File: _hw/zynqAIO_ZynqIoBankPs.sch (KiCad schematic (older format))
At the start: 70 parts, among them J201 Conn_01x03_Male, J202 Conn_01x03_Male, U201 xc7z010clg400, U202 DSC1121

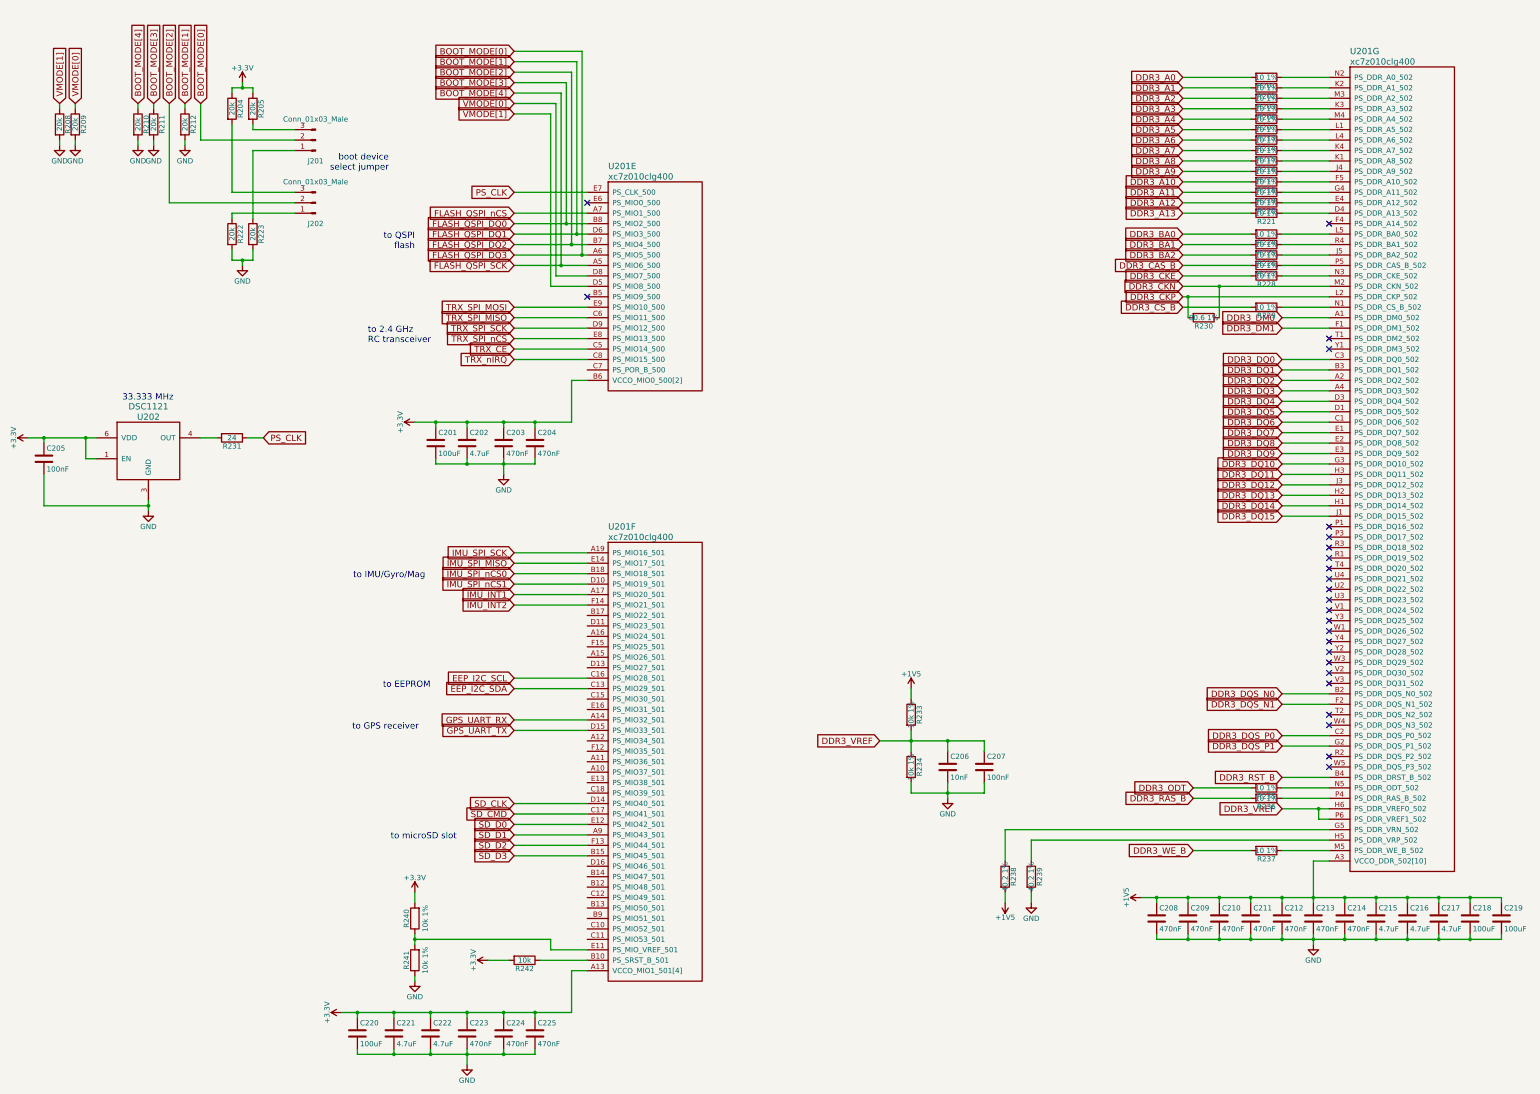
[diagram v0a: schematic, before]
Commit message: Removed Zybo board part. Not needed and complicates project setup.
Configured DDR3 to 16-bit width (using only 1 of the 2 DDR3 chips on Zybo but aligned more to zynqFC configuration).

Disabled Ethernet/USB. Not part of zynqFC.

Enabled SPI0 peripheral for IMU, I²C1 peripheral for EEPROM and UART0 peripheral for GPS.
However, all three interfaces cannot be used on Zybo and will not be used in SW.

Updated HW pinning to current Zynq PS bank planning.
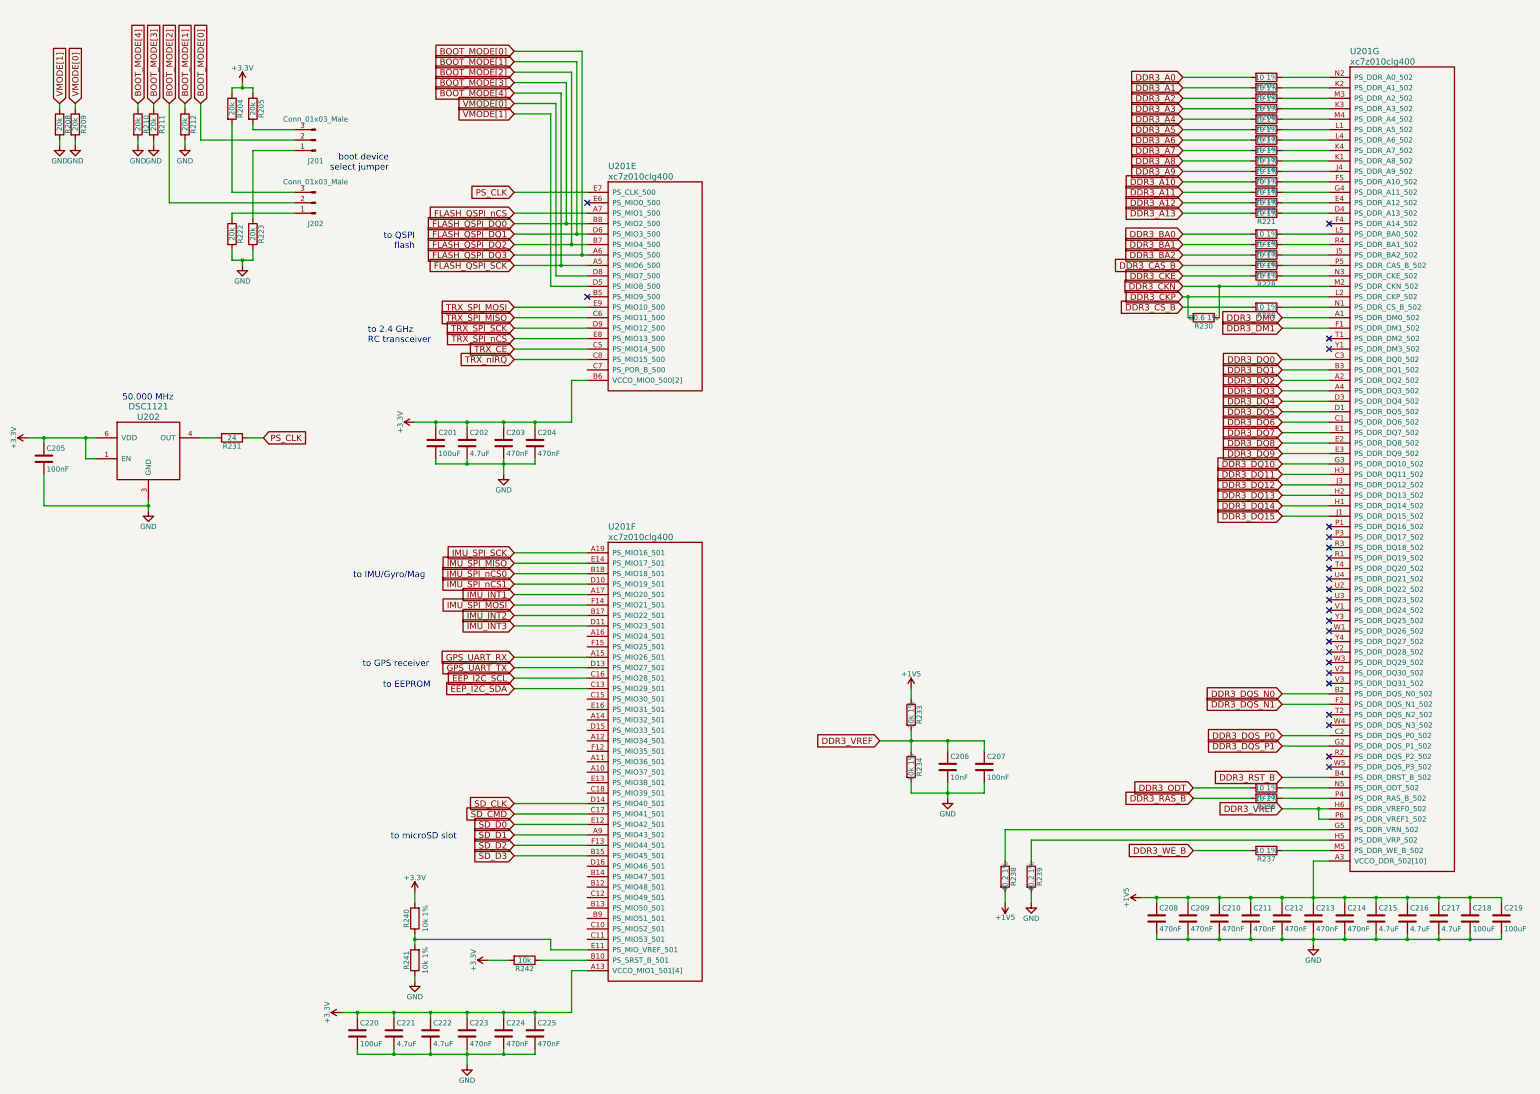
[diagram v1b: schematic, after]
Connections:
- net GPS_UART_RX: now also U201.A15 (PS_MIO26_501); no longer U201.A14 (PS_MIO32_501)
- net GPS_UART_TX: now also U201.D13 (PS_MIO27_501); no longer U201.D15 (PS_MIO33_501)
- net IMU_INT2: now also U201.B17 (PS_MIO22_501); no longer U201.F14 (PS_MIO21_501)
- net IMU_INT3: now reaches U201.D11 (PS_MIO23_501)
- new net IMU_SPI_MOSI: U201.F14 (PS_MIO21_501)
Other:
- note added: "50.000 MHz"
- note removed: "33.333 MHz"
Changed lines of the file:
@@
 Text GLabel 5450 6300 0    60   Input ~ 0
 IMU_INT1
-Text GLabel 5450 6400 0    60   Input ~ 0
+Text GLabel 5450 6500 0    60   Input ~ 0
 IMU_INT2
 Text GLabel 12800 4050 0    60   Input ~ 0
@@
 	4700 5000 4700 5050
 Wire Wire Line
-	4700 5050 5650 5050
+	4700 5050 5000 5050
 Wire Wire Line
 	5650 5050 5650 5000
 Wire Wire Line
-	5350 5000 5350 5150
+	5350 5000 5350 5050
 Connection ~ 5350 5050
 Wire Wire Line
@@
 Connection ~ 5000 5050
 Wire Wire Line
-	4500 4650 6000 4650
+	4500 4650 4700 4650
 Wire Wire Line
 	6000 4650 6000 4250
@@
 Connection ~ 4700 4650
 Wire Wire Line
-	3950 10700 5650 10700
+	3950 10700 4300 10700
 Wire Wire Line
 	5650 10700 5650 10650
@@
 Connection ~ 5350 10700
 Wire Wire Line
-	5000 10650 5000 10800
+	5000 10650 5000 10700
 Connection ~ 5000 10700
 Wire Wire Line
-	3800 10300 6000 10300
+	3800 10300 3950 10300
 Wire Wire Line
 	6000 10300 6000 9900
@@
 	5800 9600 4500 9600
 Wire Wire Line
-	4500 9550 4500 9650
+	4500 9550 4500 9600
 Connection ~ 4500 9600
 Wire Wire Line
@@
 	6150 4050 5450 4050
 Wire Wire Line
-	5450 3150 6150 3150
+	5450 3150 5900 3150
 Wire Wire Line
 	5450 2650 6150 2650
 Wire Wire Line
-	5450 2750 6150 2750
-Wire Wire Line
-	5450 2850 6150 2850
-Wire Wire Line
-	5450 2950 6150 2950
-Wire Wire Line
-	5450 3050 6150 3050
+	5450 2750 5950 2750
+Wire Wire Line
+	5450 2850 6050 2850
+Wire Wire Line
+	5450 2950 6000 2950
+Wire Wire Line
+	5450 3050 6100 3050
 Wire Wire Line
 	6100 1100 6100 3050
@@
 	2750 3000 2750 3100
 Wire Wire Line
-	2750 3100 2950 3100
+	2750 3100 2850 3100
 Wire Wire Line
 	2950 3100 2950 3000
@@
 	2750 1500 2750 1450
 Wire Wire Line
-	2750 1450 2950 1450
+	2750 1450 2850 1450
 Wire Wire Line
 	2850 1450 2850 1400
@@
 	5450 6100 6150 6100
 Wire Wire Line
-	5450 6400 6150 6400
+	5450 6500 6150 6500
 Wire Wire Line
 	5450 6200 6150 6200
@@
 	12800 7350 13250 7350
 Wire Wire Line
-	11450 9200 14900 9200
-Wire Wire Line
-	13100 8850 13100 9250
+	11450 9200 11600 9200
+Wire Wire Line
+	13100 8850 13100 9200
 Wire Wire Line
 	13100 8850 13250 8850
@@
 	12800 3250 13250 3250
 Wire Wire Line
-	11850 3350 13250 3350
-Wire Wire Line
-	11850 3450 13250 3450
+	11850 3350 12200 3350
+Wire Wire Line
+	11850 3450 11900 3450
 Wire Wire Line
 	12800 3550 13250 3550
@@
 	13150 8450 13150 8350
 Wire Wire Line
-	12800 8350 13250 8350
+	12800 8350 13150 8350
 Connection ~ 13150 8350
 Wire Wire Line
-	8950 7700 9950 7700
-Wire Wire Line
-	9250 7600 9250 7800
+	8950 7700 9250 7700
+Wire Wire Line
+	9250 7600 9250 7700
 Connection ~ 9250 7700
 Wire Wire Line
@@
 	9250 8200 9250 8100
 Wire Wire Line
-	9250 8200 9950 8200
-Wire Wire Line
-	9600 8100 9600 8250
+	9250 8200 9600 8200
+Wire Wire Line
+	9600 8100 9600 8200
 Connection ~ 9600 8200
 Wire Wire Line
@@
 	950  4850 950  4800
 Wire Wire Line
-	800  4800 1450 4800
+	800  4800 950  4800
 Wire Wire Line
 	1450 5000 1350 5000
@@
 	950  5450 1950 5450
 Wire Wire Line
-	1950 5400 1950 5500
+	1950 5400 1950 5450
 Connection ~ 1950 5450
 Connection ~ 950  4800
@@
 	11600 9550 11600 9600
 Wire Wire Line
-	11600 9600 14900 9600
+	11600 9600 11900 9600
 Wire Wire Line
 	14900 9600 14900 9550
@@
 Connection ~ 13700 9600
 Wire Wire Line
-	13100 9550 13100 9650
+	13100 9550 13100 9600
 Connection ~ 13100 9600
 Wire Wire Line
@@
 Text GLabel 5450 6200 0    60   Input ~ 0
 IMU_SPI_nCS1
-Text GLabel 5450 7600 0    60   Input ~ 0
+Text GLabel 5450 7000 0    60   Input ~ 0
 GPS_UART_TX
-Text GLabel 5450 7500 0    60   Input ~ 0
+Text GLabel 5450 6900 0    60   Input ~ 0
 GPS_UART_RX
 Wire Wire Line
-	5450 7500 6150 7500
-Wire Wire Line
-	5450 7600 6150 7600
-Text Notes 3900 7600 0    60   ~ 0
+	5450 6900 6150 6900
+Wire Wire Line
+	5450 7000 6150 7000
+Text Notes 4000 7000 0    60   ~ 0
 to GPS receiver
 Text Notes 1700 4450 0    60   ~ 0
-33.333 MHz
+50.000 MHz
+Wire Wire Line
+	5350 5050 5650 5050
+Wire Wire Line
+	5350 5050 5350 5150
+Wire Wire Line
+	5000 5050 5350 5050
+Wire Wire Line
+	5650 4650 6000 4650
+Wire Wire Line
+	5350 4650 5650 4650
+Wire Wire Line
+	5000 4650 5350 4650
+Wire Wire Line
+	4700 4650 5000 4650
+Wire Wire Line
+	5350 10700 5650 10700
+Wire Wire Line
+	5000 10700 5350 10700
+Wire Wire Line
+	5000 10700 5000 10800
+Wire Wire Line
+	5650 10300 6000 10300
+Wire Wire Line
+	5350 10300 5650 10300
+Wire Wire Line
+	5000 10300 5350 10300
+Wire Wire Line
+	3950 10300 4300 10300
+Wire Wire Line
+	4300 10300 4650 10300
+Wire Wire Line
+	4650 10300 5000 10300
+Wire Wire Line
+	4650 10700 5000 10700
+Wire Wire Line
+	4300 10700 4650 10700
+Wire Wire Line
+	4500 9600 4500 9650
+Wire Wire Line
+	6100 3050 6150 3050
+Wire Wire Line
+	6050 2850 6150 2850
+Wire Wire Line
+	6000 2950 6150 2950
+Wire Wire Line
+	5950 2750 6150 2750
+Wire Wire Line
+	5900 3150 6150 3150
+Wire Wire Line
+	2850 3100 2950 3100
+Wire Wire Line
+	2850 1450 2950 1450
+Wire Wire Line
+	13150 8350 13250 8350
+Wire Wire Line
+	9250 7700 9600 7700
+Wire Wire Line
+	9250 7700 9250 7800
+Wire Wire Line
+	9600 8200 9950 8200
+Wire Wire Line
+	9600 8200 9600 8250
+Wire Wire Line
+	9600 7700 9950 7700
+Wire Wire Line
+	11900 3450 13250 3450
+Wire Wire Line
+	12200 3350 13250 3350
+Wire Wire Line
+	1350 4800 1450 4800
+Wire Wire Line
+	1950 5450 1950 5500
+Wire Wire Line
+	950  4800 1350 4800
+Wire Wire Line
+	13100 9200 13400 9200
+Wire Wire Line
+	13100 9200 13100 9250
+Wire Wire Line
+	14600 9200 14900 9200
+Wire Wire Line
+	14300 9200 14600 9200
+Wire Wire Line
+	14000 9200 14300 9200
+Wire Wire Line
+	13700 9200 14000 9200
+Wire Wire Line
+	13400 9200 13700 9200
+Wire Wire Line
+	12800 9200 13100 9200
+Wire Wire Line
+	12500 9200 12800 9200
+Wire Wire Line
+	12200 9200 12500 9200
+Wire Wire Line
+	11900 9200 12200 9200
+Wire Wire Line
+	11600 9200 11900 9200
+Wire Wire Line
+	14600 9600 14900 9600
+Wire Wire Line
+	14300 9600 14600 9600
+Wire Wire Line
+	14000 9600 14300 9600
+Wire Wire Line
+	13700 9600 14000 9600
+Wire Wire Line
+	13100 9600 13400 9600
+Wire Wire Line
+	13100 9600 13100 9650
+Wire Wire Line
+	13400 9600 13700 9600
+Wire Wire Line
+	12800 9600 13100 9600
+Wire Wire Line
+	12500 9600 12800 9600
+Wire Wire Line
+	12200 9600 12500 9600
+Wire Wire Line
+	11900 9600 12200 9600
+Text GLabel 5450 6400 0    60   Input ~ 0
+IMU_SPI_MOSI
+Wire Wire Line
+	5450 6400 6150 6400
+Text GLabel 5450 6600 0    60   Input ~ 0
+IMU_INT3
+Wire Wire Line
+	5450 6600 6150 6600
 $EndSCHEMATC
